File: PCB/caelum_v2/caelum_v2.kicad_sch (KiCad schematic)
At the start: 36 parts, among them J1 SS445P, J2 i2C Bus2, J3 Pulse1, J4 Batt, J7 I2C BUS1, J8 DS18B20, Q1 FS8205A-FC, U1 DW01A, U2 MCP1825S, U3 ESP32-H2-SUPERMINI

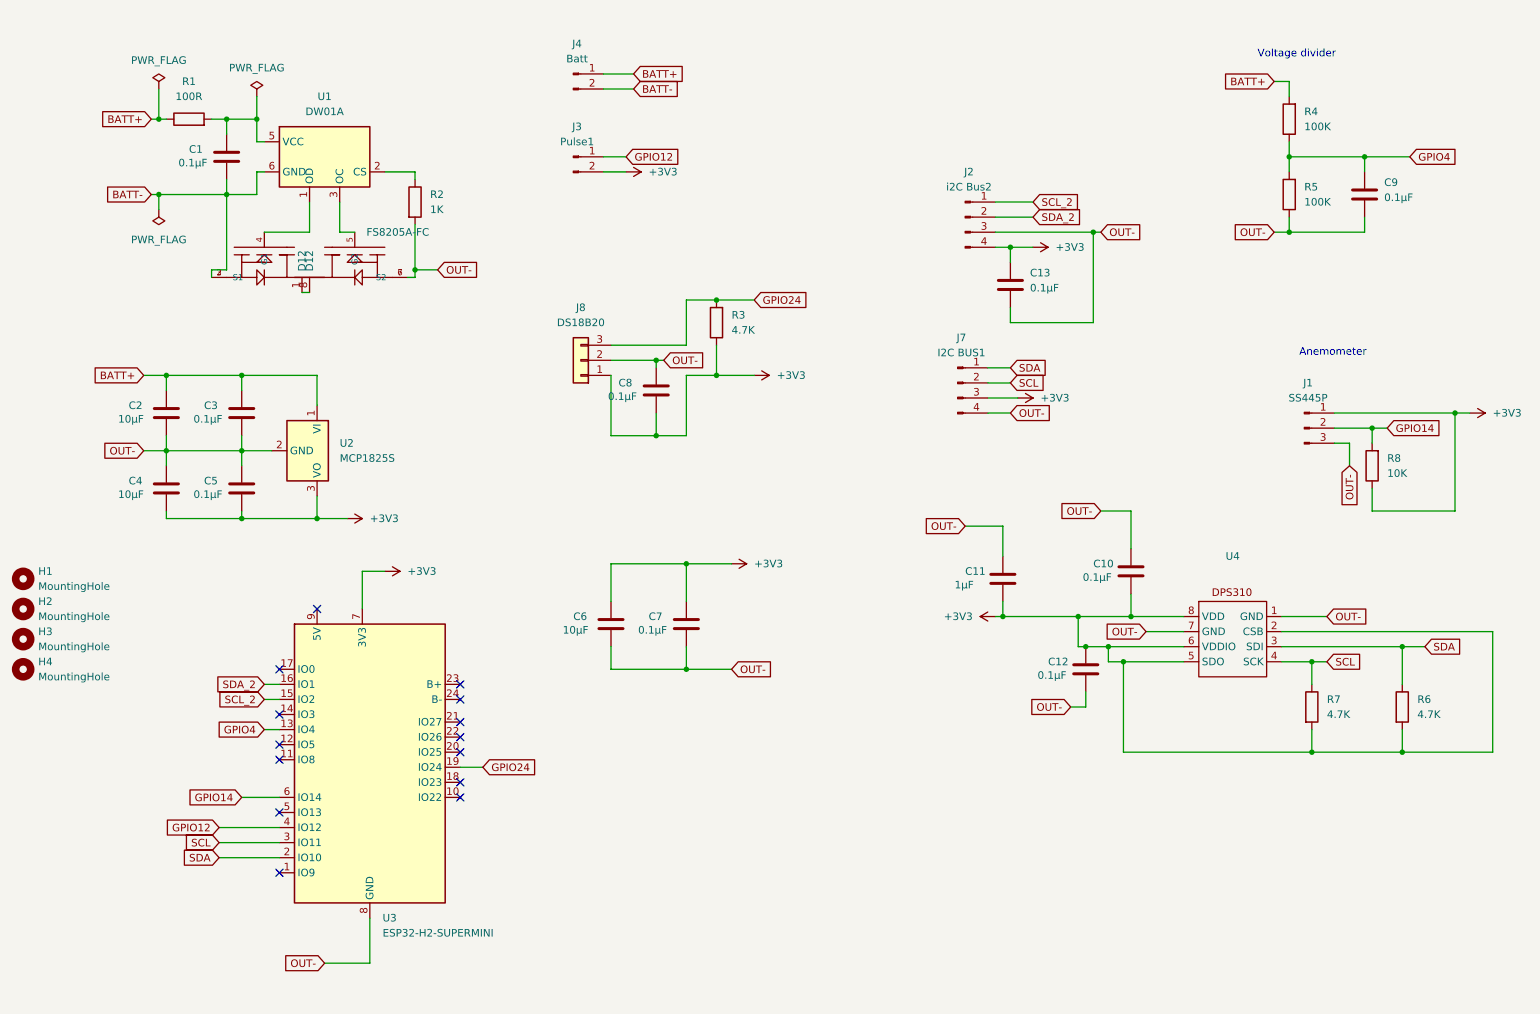
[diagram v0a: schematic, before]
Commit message: Clone of Caelum v1
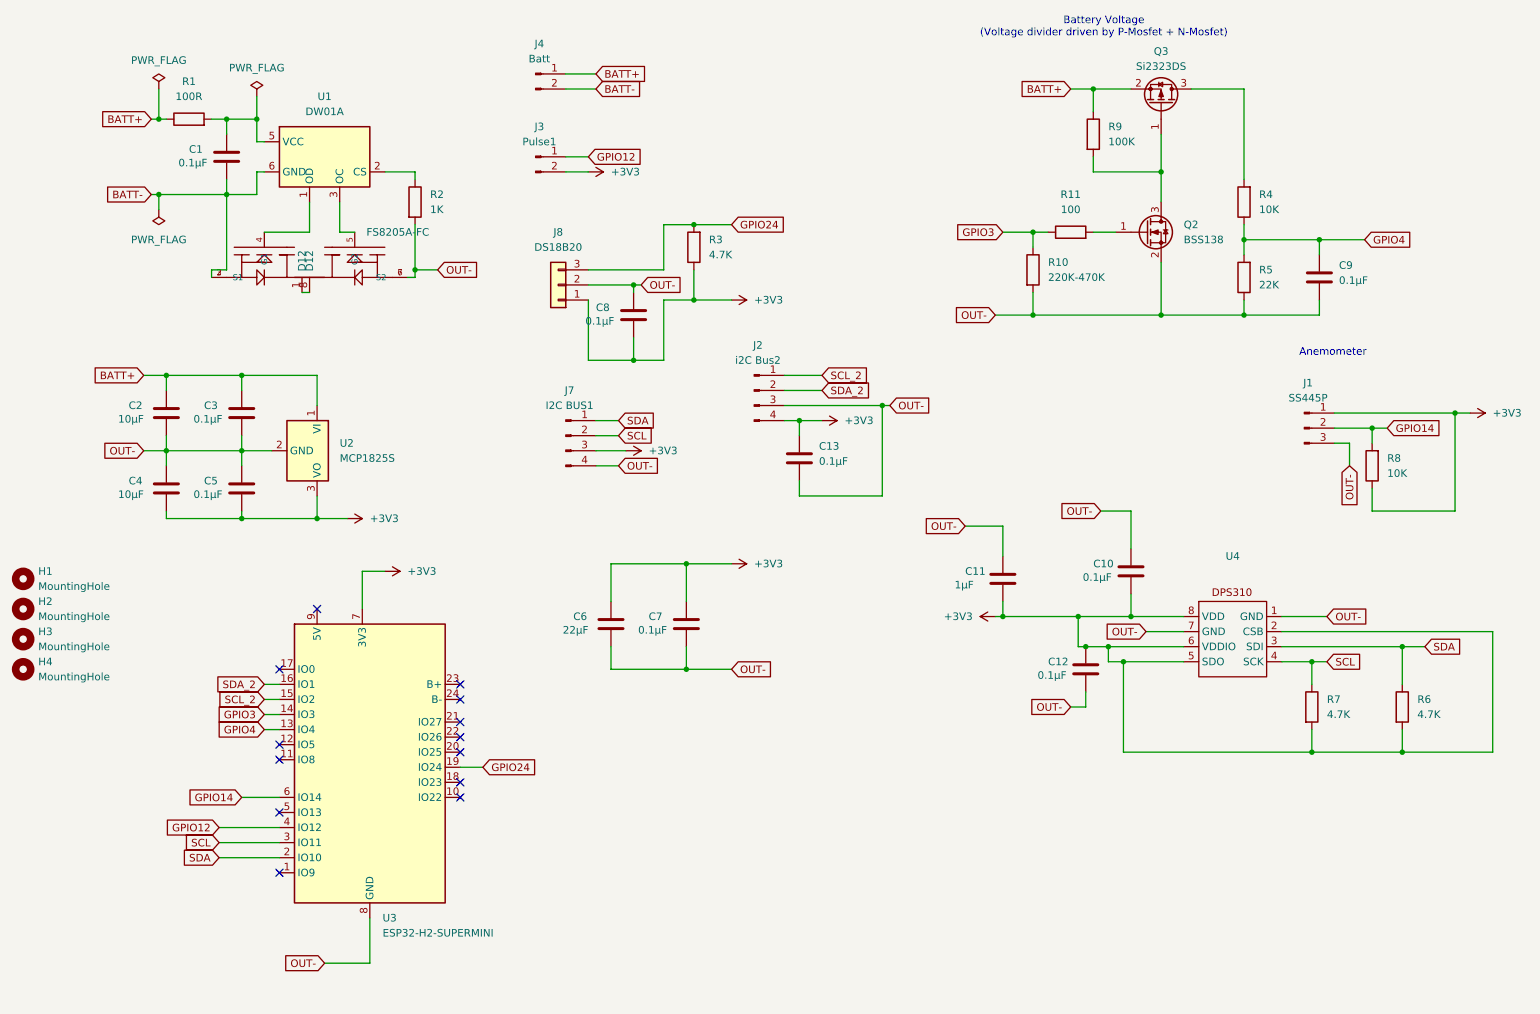
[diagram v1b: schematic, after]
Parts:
- added Q2: BSS138, Package_TO_SOT_SMD:SOT-23, symbol Transistor_FET:BSS138
- added Q3: Si2323DS, Package_TO_SOT_SMD:SOT-23, symbol Transistor_FET:Q_PMOS_GSD
- added R10: 220K-470K, Resistor_SMD:R_0805_2012Metric, symbol Device:R
- added R11: 100, Resistor_SMD:R_0805_2012Metric, symbol Device:R
- added R9: 100K, Resistor_SMD:R_0805_2012Metric, symbol Device:R
- C6: value 10µF -> 22µF
- R4: value 100K -> 10K
- R5: value 100K -> 22K
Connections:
- net BATT+: now also Q3.2 (S), R9.1; no longer R4.2
- net OUT-: now also Q2.2 (S), R10.2
- net GPIO3: now reaches U3.14 (IO3)
- net GPIO3: now also R10.1, R11.1
- new net: Q3.3 (D), R4.2
- new net: Q2.3 (D), Q3.1 (G), R9.2
- new net: Q2.1 (G), R11.2
- no-connect marks 14 -> 13
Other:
- note added: "Battery Voltage (Voltage divider driven by P-Mosfet + N-Mosfet)"
- note removed: "Voltage divider"
- moved on the sheet: C13, C8, C9, J2, J3, J4, J7, J8, R3, R4, R5

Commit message: Add ESP32 symbol and wind vane macro; update library paths
- Updated the library path for "caelum_v2" in fp-lib-table.
- Added ESP32 symbol to sym-lib-table for better component management.
- Created a new FreeCAD macro for generating a wind vane assembly compatible with the AS5600 sensor, including detailed parameters and assembly instructions.
- Introduced various components such as the rotating shaft, magnet holder, wind vane, arrow pointer, counterweight, central body, base mount, and sensor mount area.
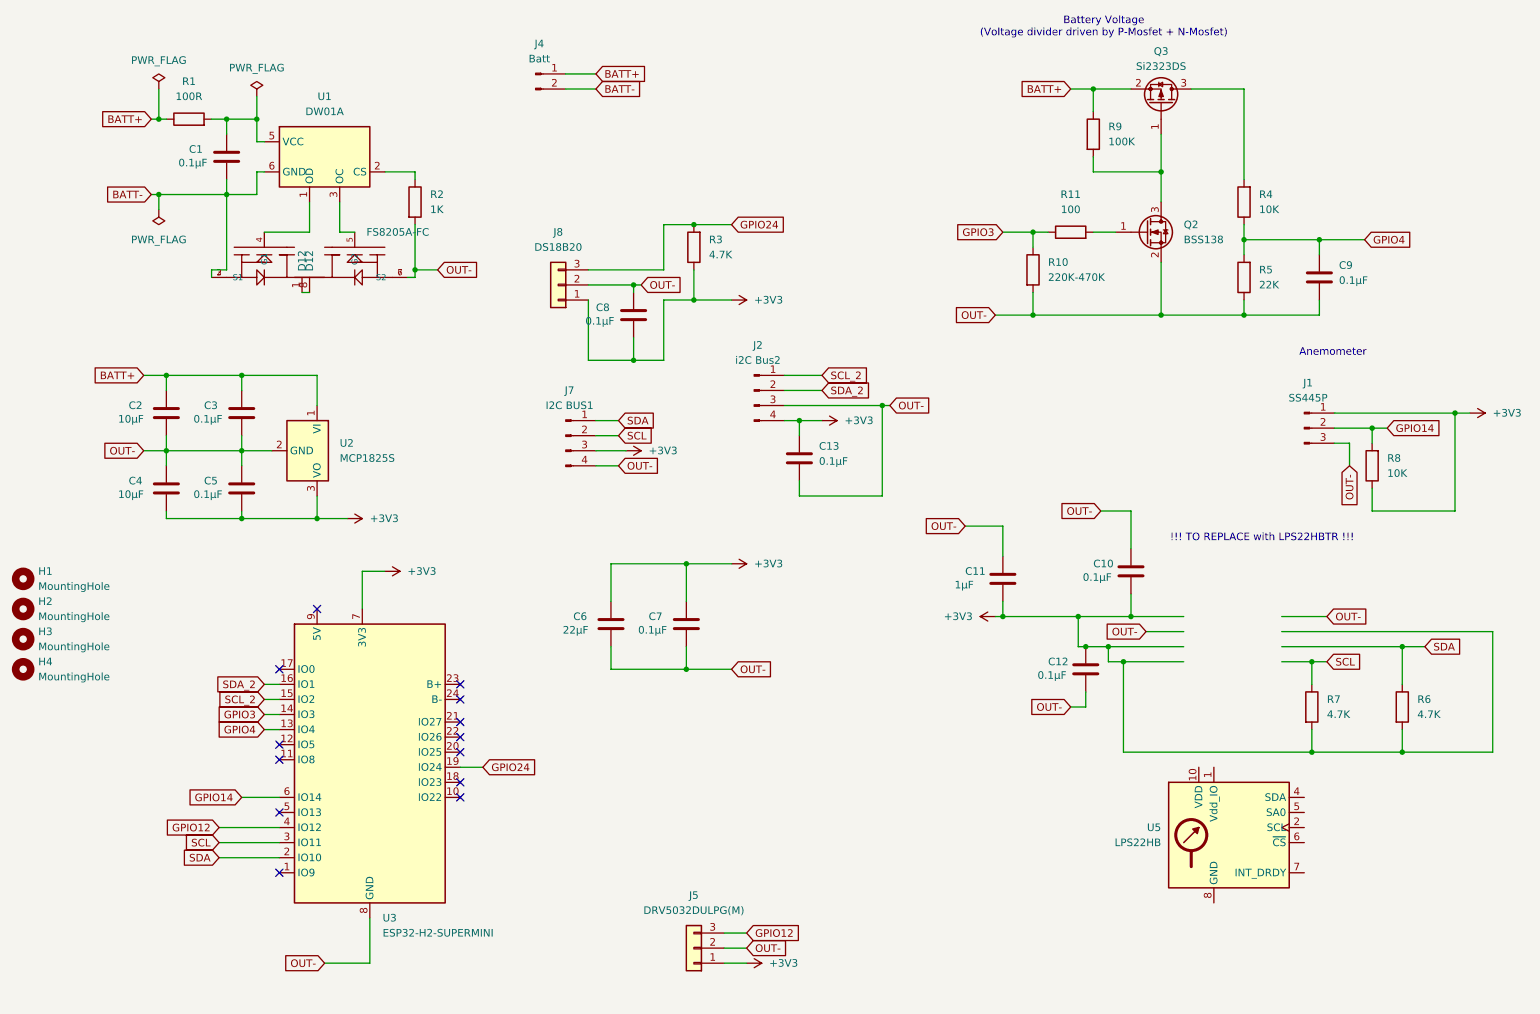
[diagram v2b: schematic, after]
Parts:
- removed J3: Pulse1, Connector_Hirose:Hirose_DF13C_CL535-0402-2-51_1x02-1MP_P1.25mm_Vertical, symbol Connector:Conn_01x02_Pin
- removed U4: ~, Package_LGA:Bosch_LGA-8_2x2.5mm_P0.65mm_ClockwisePinNumbering, symbol caelum:DPS310
- added J5: DRV5032DULPG(M), Connector_Hirose:Hirose_DF13C_CL535-0403-5-51_1x03-1MP_P1.25mm_Vertical, symbol Connector_Generic:Conn_01x03
- added U5: LPS22HB, Package_LGA:ST_HLGA-10_2x2mm_P0.5mm_LayoutBorder3x2y, symbol Sensor_Pressure:LPS22HB
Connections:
- net +3V3: now also J5.1 (Pin_1)
- net GPIO12: now also J5.3 (Pin_3)
- net OUT-: now also J5.2 (Pin_2)
- new net: U5.3 (GND), U5.8 (GND), U5.9 (GND)
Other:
- note added: "!!! TO REPLACE with LPS22HBTR !!!"
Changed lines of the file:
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@@
 		)
 	)
+	(text "!!! TO REPLACE with LPS22HBTR !!!"
+		(exclude_from_sim no)
+		(at 227.838 102.362 0)
+		(effects
+			(font
+				(size 1.27 1.27)
+			)
+		)
+	)
 	(text "Battery Voltage \n(Voltage divider driven by P-Mosfet + N-Mosfet)"
 		(exclude_from_sim no)
@@
 	(wire
 		(pts
+			(xy 137.16 168.91) (xy 140.97 168.91)
+		)
+		(stroke
+			(width 0)
+			(type default)
+		)
+	)
+	(wire
+		(pts
 			(xy 83.82 58.42) (xy 85.09 58.42)
 		)
@@
 	(wire
 		(pts
+			(xy 137.16 173.99) (xy 140.97 173.99)
+		)
+		(stroke
+			(width 0)
+			(type default)
+		)
+	)
+	(wire
+		(pts
 			(xy 147.32 74.93) (xy 153.67 74.93)
 		)
@@
 	(wire
 		(pts
-			(xy 110.49 38.1) (xy 114.3 38.1)
-		)
-		(stroke
-			(width 0)
-			(type default)
-		)
-	)
-	(wire
-		(pts
 			(xy 214.63 123.19) (xy 204.47 123.19)
 		)
@@
 	(wire
 		(pts
-			(xy 110.49 40.64) (xy 114.3 40.64)
+			(xy 137.16 171.45) (xy 140.97 171.45)
 		)
 		(stroke
@@
 		)
 	)
+	(global_label "OUT-"
+		(shape input)
+		(at 140.97 171.45 0)
+		(fields_autoplaced yes)
+		(effects
+			(font
+				(size 1.27 1.27)
+			)
+			(justify left)
+		)
+		(property "Intersheetrefs" "${INTERSHEET_REFS}"
+			(at 149.1562 171.45 0)
+			(effects
+				(font
+					(size 1.27 1.27)
+				)
+				(justify left)
+				(hide yes)
+			)
+		)
+	)
 	(global_label "GPIO4"
 		(shape input)
@@
 	(global_label "GPIO12"
 		(shape input)
-		(at 114.3 38.1 0)
+		(at 140.97 168.91 0)
 		(fields_autoplaced yes)
 		(effects
@@
 		)
 		(property "Intersheetrefs" "${INTERSHEET_REFS}"
-			(at 124.1795 38.1 0)
+			(at 150.8495 168.91 0)
 			(effects
 				(font
@@
 	)
 	(symbol
+		(lib_id "Sensor_Pressure:LPS22HB")
+		(at 222.25 153.67 0)
+		(unit 1)
+		(exclude_from_sim no)
+		(in_bom yes)
+		(on_board yes)
+		(dnp no)
+		(fields_autoplaced yes)
+		(property "Reference" "U5"
+			(at 210.82 151.1299 0)
+			(effects
+				(font
+					(size 1.27 1.27)
+				)
+				(justify right)
+			)
+		)
+		(property "Value" "LPS22HB"
+			(at 210.82 153.6699 0)
+			(effects
+				(font
+					(size 1.27 1.27)
+				)
+				(justify right)
+			)
+		)
+		(property "Footprint" "Package_LGA:ST_HLGA-10_2x2mm_P0.5mm_LayoutBorder3x2y"
+			(at 223.52 165.1 0)
+			(effects
+				(font
+					(size 1.27 1.27)
+				)
+				(justify left)
+				(hide yes)
+			)
+		)
+		(property "Datasheet" "https://www.st.com/resource/en/datasheet/lps22hb.pdf"
+			(at 223.52 167.64 0)
+			(effects
+				(font
+					(size 1.27 1.27)
+				)
+				(justify left)
+				(hide yes)
+			)
+		)
+		(property "Description" "MEMS nano pressure sensor, 260-1260 hPa, absolute digital output baromeeter, 24 bit, SPI, I2C, 0.0075 hPa noise rms, ST_HLGA-10L"
+			(at 222.25 153.67 0)
+			(effects
+				(font
+					(size 1.27 1.27)
+				)
+				(hide yes)
+			)
+		)
+		(pin "4"
+		)
+		(pin "9"
+		)
+		(pin "7"
+		)
+		(pin "1"
+		)
+		(pin "3"
+		)
+		(pin "8"
+		)
+		(pin "2"
+		)
+		(pin "5"
+		)
+		(pin "6"
+		)
+		(pin "10"
+		)
+		(instances
+			(project ""
+				(path "/37ad57cb-45d9-40ac-b6d6-3143604b7b27"
+					(reference "U5")
+					(unit 1)
+				)
+			)
+		)
+	)
+	(symbol
 		(lib_id "Device:C")
 		(at 53.34 38.1 0)
@@
 	(symbol
 		(lib_id "power:+3V3")
-		(at 114.3 40.64 270)
+		(at 140.97 173.99 270)
 		(unit 1)
 		(exclude_from_sim no)
@@
 		(fields_autoplaced yes)
 		(property "Reference" "#PWR04"
-			(at 110.49 40.64 0)
+			(at 137.16 173.99 0)
 			(effects
 				(font
@@
 		)
 		(property "Value" "+3V3"
-			(at 118.11 40.6399 90)
+			(at 144.78 173.9899 90)
 			(effects
 				(font
@@
 		)
 		(property "Footprint" ""
-			(at 114.3 40.64 0)
+			(at 140.97 173.99 0)
 			(effects
 				(font
@@
 		)
 		(property "Datasheet" ""
-			(at 114.3 40.64 0)
+			(at 140.97 173.99 0)
 			(effects
 				(font
@@
 		)
 		(property "Description" "Power symbol creates a global label with name \"+3V3\""
-			(at 114.3 40.64 0)
+			(at 140.97 173.99 0)
 			(effects
 				(font
@@
 	)
 	(symbol
-		(lib_id "caelum:DPS310")
-		(at 223.52 120.65 0)
-		(unit 1)
-		(exclude_from_sim no)
-		(in_bom yes)
-		(on_board yes)
-		(dnp no)
-		(fields_autoplaced yes)
-		(property "Reference" "U4"
-			(at 222.885 105.41 0)
-			(effects
-				(font
-					(size 1.27 1.27)
-				)
-			)
-		)
-		(property "Value" "~"
-			(at 222.885 107.95 0)
-			(effects
-				(font
-					(size 1.27 1.27)
-				)
-				(hide yes)
-			)
-		)
-		(property "Footprint" "Package_LGA:Bosch_LGA-8_2x2.5mm_P0.65mm_ClockwisePinNumbering"
-			(at 223.52 120.65 0)
-			(effects
-				(font
-					(size 1.27 1.27)
-				)
-				(hide yes)
-			)
-		)
-		(property "Datasheet" ""
-			(at 223.52 120.65 0)
-			(effects
-				(font
-					(size 1.27 1.27)
-				)
-				(hide yes)
-			)
-		)
-		(property "Description" ""
-			(at 223.52 120.65 0)
-			(effects
-				(font
-					(size 1.27 1.27)
-				)
-				(hide yes)
-			)
-		)
-		(pin "2"
-		)
-		(pin "3"
-		)
-		(pin "6"
-		)
-		(pin "1"
-		)
-		(pin "5"
-		)
-		(pin "7"
-		)
-		(pin "4"
-		)
-		(pin "8"
-		)
-		(instances
-			(project ""
-				(path "/37ad57cb-45d9-40ac-b6d6-3143604b7b27"
-					(reference "U4")
-					(unit 1)
-				)
-			)
-		)
-	)
-	(symbol
 		(lib_id "Device:C")
 		(at 149.86 88.9 0)
@@
 	)
 	(symbol
-		(lib_id "Connector:Conn_01x02_Pin")
-		(at 105.41 38.1 0)
+		(lib_id "Connector_Generic:Conn_01x03")
+		(at 132.08 171.45 180)
 		(unit 1)
 		(exclude_from_sim no)
@@
 		(dnp no)
 		(fields_autoplaced yes)
-		(property "Reference" "J3"
-			(at 106.045 33.02 0)
+		(property "Reference" "J5"
+			(at 132.08 162.56 0)
 			(effects
 				(font
@@
 			)
 		)
-		(property "Value" "Pulse1"
-			(at 106.045 35.56 0)
+		(property "Value" "DRV5032DULPG(M)"
+			(at 132.08 165.1 0)
 			(effects
 				(font
@@
 			)
 		)
-		(property "Footprint" "Connector_Hirose:Hirose_DF13C_CL535-0402-2-51_1x02-1MP_P1.25mm_Vertical"
-			(at 105.41 38.1 0)
+		(property "Footprint" "Connector_Hirose:Hirose_DF13C_CL535-0403-5-51_1x03-1MP_P1.25mm_Vertical"
+			(at 132.08 171.45 0)
 			(effects
 				(font
@@
 		)
 		(property "Datasheet" "~"
-			(at 105.41 38.1 0)
+			(at 132.08 171.45 0)
 			(effects
 				(font
@@
 			)
 		)
-		(property "Description" "Generic connector, single row, 01x02, script generated"
-			(at 105.41 38.1 0)
+		(property "Description" "Generic connector, single row, 01x03, script generated (kicad-library-utils/schlib/autogen/connector/)"
+			(at 132.08 171.45 0)
 			(effects
 				(font
@@
 			)
 		)
+		(pin "3"
+		)
 		(pin "2"
 		)
@@
 		)
 		(instances
-			(project ""
+			(project "caelum_v2"
 				(path "/37ad57cb-45d9-40ac-b6d6-3143604b7b27"
-					(reference "J3")
+					(reference "J5")
 					(unit 1)
 				)

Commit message: Refactor code structure for improved readability and maintainability
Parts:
- removed C12: 0.1µF, Capacitor_SMD:C_0805_2012Metric, symbol Device:C
- J1, J5, J8: footprint Connector_Hirose:Hirose_DF13C_CL535-0403-5-51_1x03-1MP_P1.25mm_Vertical -> Connector_JST:JST_PH_B3B-PH-SM4-TB_1x03-1MP_P2.00mm_Vertical
- J2: footprint Connector_JST:JST_PH_B4B-PH-SM4-TB_1x04-1MP_P2.00mm_Vertical -> Connector_JST:JST_PH_S4B-PH-SM4-TB_1x04-1MP_P2.00mm_Horizontal
- J4: footprint Connector_PinHeader_2.54mm:PinHeader_1x02_P2.54mm_Vertical -> Connector_JST:JST_PH_S2B-PH-SM4-TB_1x02-1MP_P2.00mm_Horizontal
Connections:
- net +3V3: now also C13.2, J1.3 (Pin_3), J2.2 (Pin_2), J5.3 (Pin_3), J7.2 (Pin_2), J8.3 (Pin_3), U5.1 (Vdd_IO), U5.10 (VDD), U5.5 (SA0), U5.6 (~{CS}); no longer C13.1, J1.1 (Pin_1), J2.4 (Pin_4), J5.1 (Pin_1), J7.3 (Pin_3), J8.1 (Pin_1)
- net GPIO12: now also U5.7 (INT_DRDY); no longer J5.3 (Pin_3)
- net GPIO14: now also J1.1 (Pin_1); no longer J1.2 (Pin_2)
- net GPIO24: now also J8.1 (Pin_1); no longer J8.3 (Pin_3)
- net OUT-: now also C13.1, J1.2 (Pin_2), J2.1 (Pin_1), J7.1 (Pin_1), U5.3 (GND), U5.8 (GND), U5.9 (GND); no longer C13.2, J1.3 (Pin_3), J2.3 (Pin_3), J7.4 (Pin_4)
- net SCL: now also J7.4 (Pin_4), U5.2 (SCL); no longer J7.2 (Pin_2)
- net SCL_2: now also J2.4 (Pin_4); no longer J2.1 (Pin_1)
- net SDA: now also J7.3 (Pin_3), U5.4 (SDA); no longer J7.1 (Pin_1)
- net SDA_2: now also J2.3 (Pin_3); no longer J2.2 (Pin_2)
- net GPIO13: now reaches U3.5 (IO13)
- net GPIO13: now also J5.1 (Pin_1)
- no-connect marks 13 -> 12
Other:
- moved on the sheet: C13, J1, J8, R8, U5
